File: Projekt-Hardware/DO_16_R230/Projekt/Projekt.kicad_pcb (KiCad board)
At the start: 2 copper layers, 131.6 x 142.2 mm, 41 parts, among them J1 COM_Bus, J2 COM_Bus, J4 Conn_01x02, J5 Conn_01x08, J6 Conn_01x08, K1 DIPxx-1Cxx-51x, K10 DIPxx-1Cxx-51x, K11 DIPxx-1Cxx-51x, K12 DIPxx-1Cxx-51x, K13 DIPxx-1Cxx-51x, K14 DIPxx-1Cxx-51x, K15 DIPxx-1Cxx-51x, K16 DIPxx-1Cxx-51x, K2 DIPxx-1Cxx-51x, K3 DIPxx-1Cxx-51x, K4 DIPxx-1Cxx-51x, K5 DIPxx-1Cxx-51x, K6 DIPxx-1Cxx-51x, K7 DIPxx-1Cxx-51x, K8 DIPxx-1Cxx-51x, K9 DIPxx-1Cxx-51x, SW1 RESET, U1 ATmega328P-PU

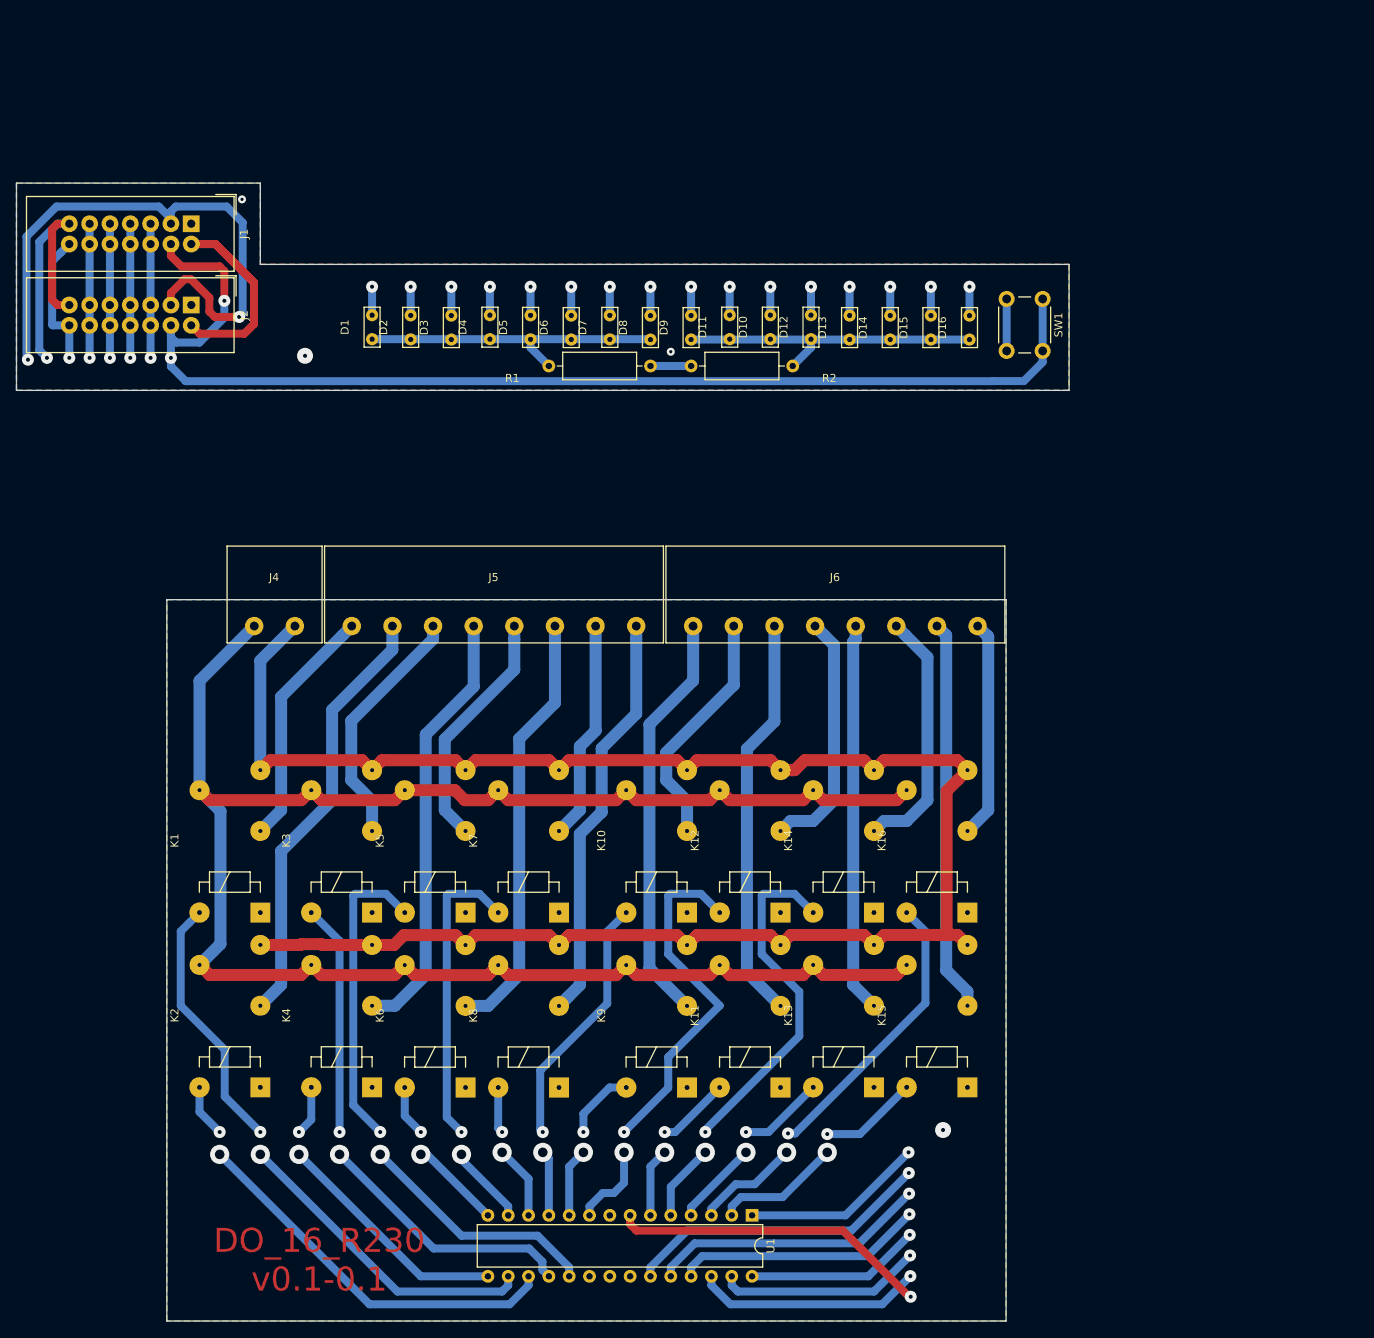
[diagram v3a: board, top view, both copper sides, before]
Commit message: Anpassungen Gehäuse + CNC Experimente
Anpassungen des Gehäuses an die Leiteplatte

Angefangen mit Tests für das herstellen der Leiterplatte mit einer CNC Fräse
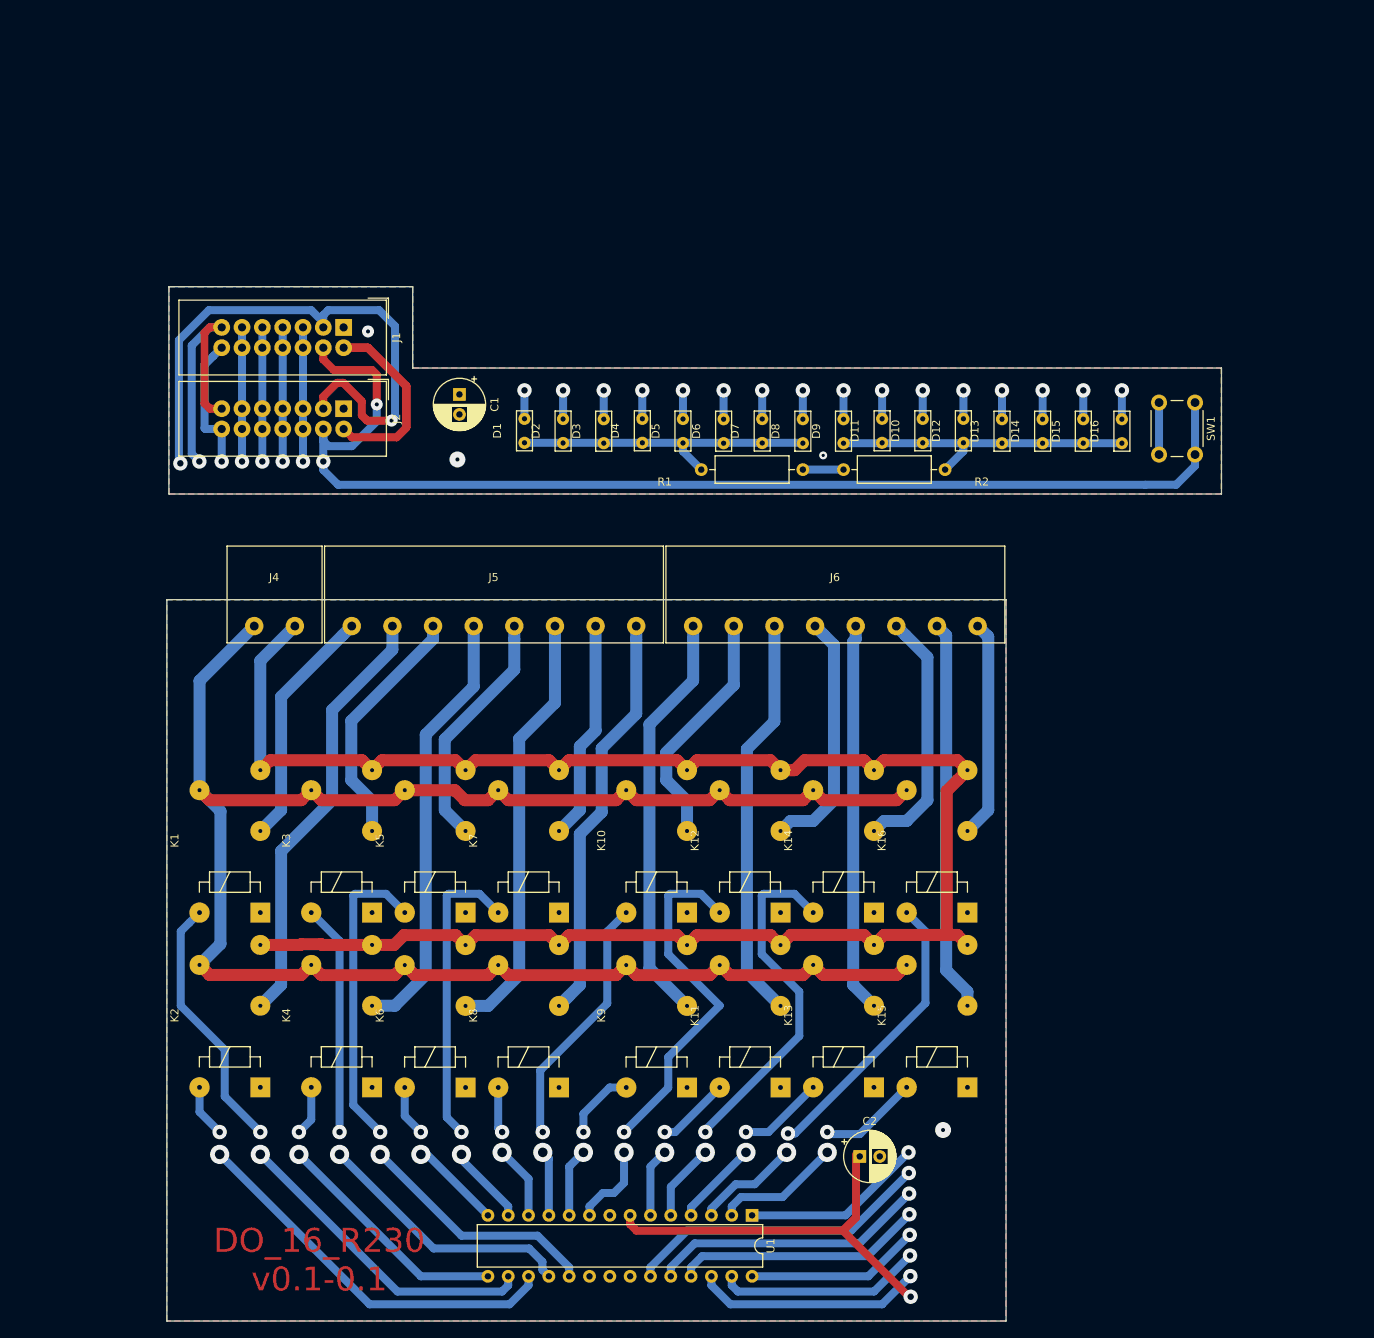
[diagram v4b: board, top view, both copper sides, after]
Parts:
- added C1: 10uF, Capacitor_THT:CP_Radial_D6.3mm_P2.50mm, F.Cu at (97.8, 71.9)
- added C2: 10uF, Capacitor_THT:CP_Radial_D6.3mm_P2.50mm, F.Cu at (147.8, 167.1)
- moved D1 23.0 mm to (105.9, 76.4)
- moved D10 23.0 mm to (155.7, 76.4)
- moved D11 23.0 mm to (150.6, 76.4)
- moved D12 23.0 mm to (160.8, 76.4)
- moved D4 23.0 mm to (120.7, 76.4)
- moved R2 23.0 mm to (158.5, 81.3)
- moved D13 23.0 mm to (165.6, 76.5)
- moved D15 23.0 mm to (175.8, 76.5)
- moved D8 23.0 mm to (140.7, 76.5)
- moved SW1 23.0 mm to (189.7, 72.9)
- moved R1 23.0 mm to (128.0, 81.3)
- moved J1 23.0 mm to (83.3, 63.5)
- moved D2 23.0 mm to (110.7, 76.5)
- moved D3 23.0 mm to (115.8, 76.5)
- moved D5 23.0 mm to (125.7, 76.5)
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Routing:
- net Net-(C2-Pad1): track 78.8 -> 89.0 mm
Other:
- board size 131.6 x 142.2 mm -> 131.8 x 129.3 mm

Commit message: Hardware CNC Codes erstellt
Fertigungsdateien für eine CNC Version der
Leiterplatten erstellt.
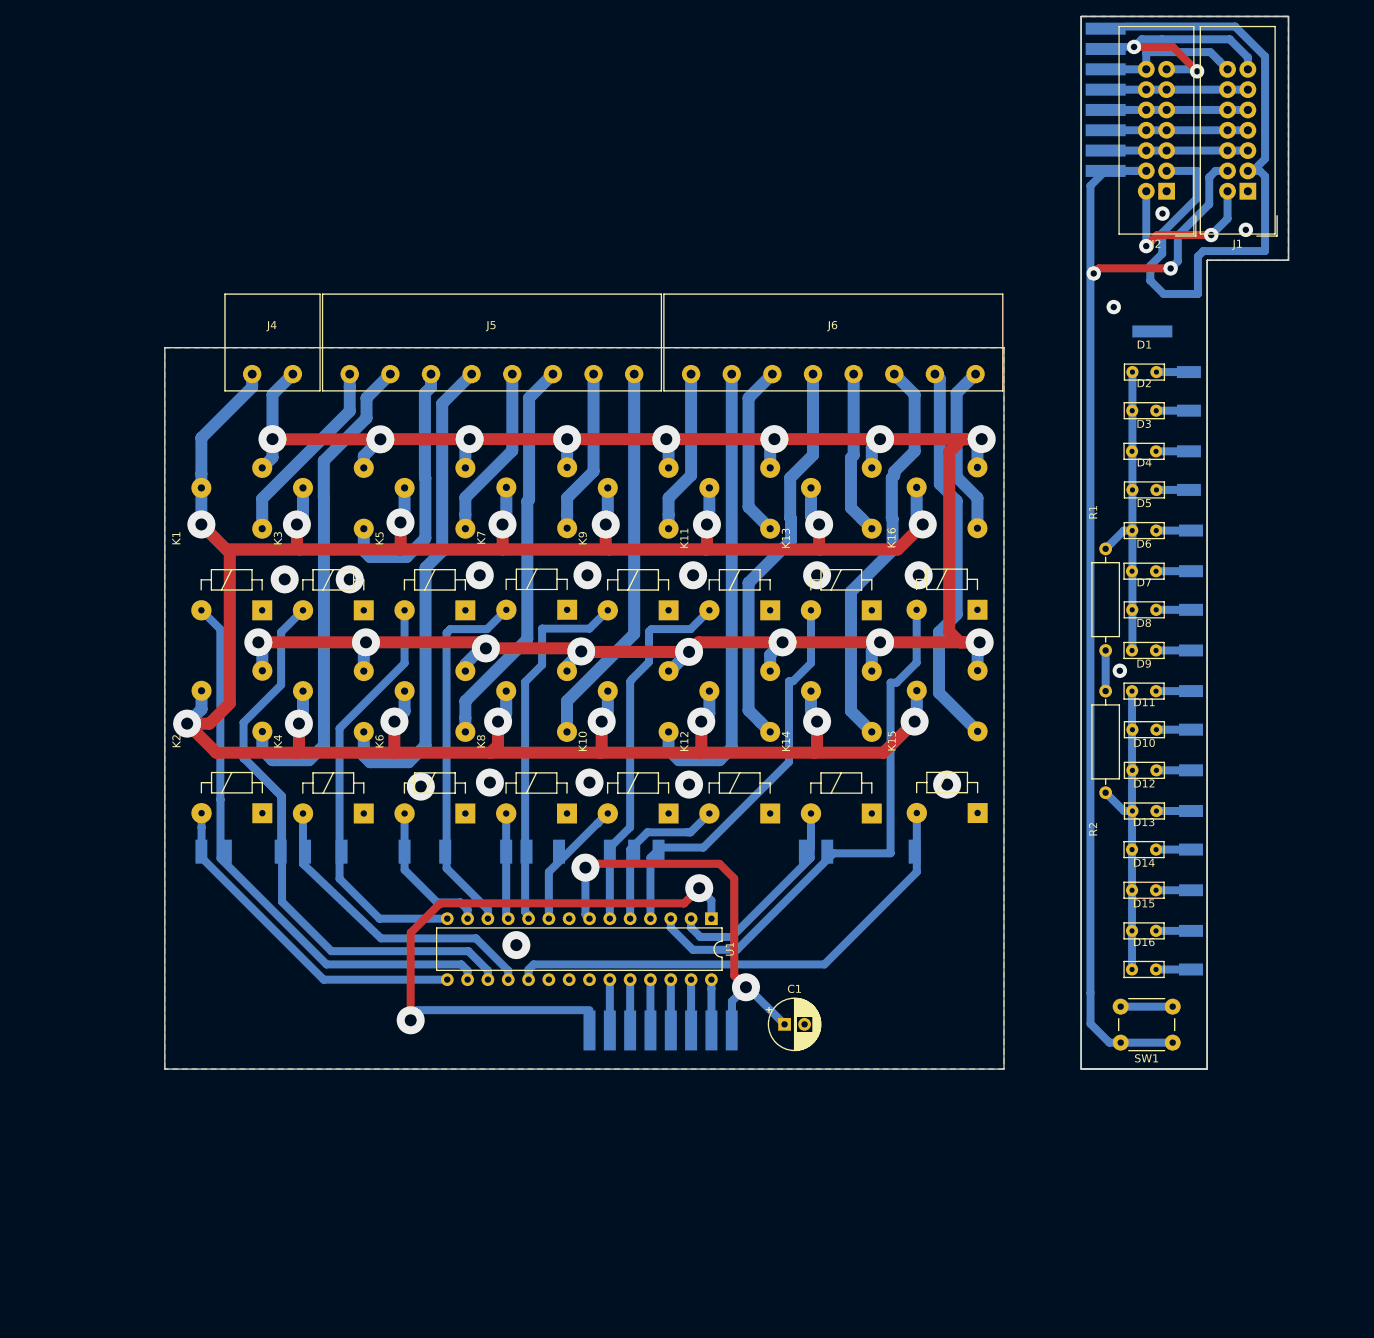
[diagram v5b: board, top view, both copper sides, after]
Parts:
- removed C2: 10uF, Capacitor_THT:CP_Radial_D6.3mm_P2.50mm
- added REF**: SM_SolderPad_1.5x3, Footprints:SM_SolderPad_1.5x3, B.Cu at (189.0, 73.9)
- added REF**: SM_SolderPad_1.5x5, Footprints:SM_SolderPad_1.5x5, B.Cu at (178.6, 33.8)
- added REF**: SM_SolderPad_1.5x5, Footprints:SM_SolderPad_1.5x5, B.Cu at (178.6, 31.2)
- added REF**: SM_SolderPad_1.5x3, Footprints:SM_SolderPad_1.5x3, B.Cu at (189.2, 118.9)
- added REF**: SM_SolderPad_1.5x3, Footprints:SM_SolderPad_1.5x3, B.Cu at (189.2, 109.0)
- added REF**: SM_SolderPad_1.5x3, Footprints:SM_SolderPad_1.5x3, B.Cu at (189.2, 98.8)
- added REF**: SM_SolderPad_1.5x3, Footprints:SM_SolderPad_1.5x3, B.Cu at (189.2, 94.0)
- added REF**: SM_SolderPad_1.5x3, Footprints:SM_SolderPad_1.5x3, B.Cu at (189.2, 103.9)
- added REF**: SM_SolderPad_1.5x3, Footprints:SM_SolderPad_1.5x3, B.Cu at (189.0, 83.8)
- added REF**: SM_SolderPad_1.5x3, Footprints:SM_SolderPad_1.5x3, B.Cu at (189.0, 69.1)
- added REF**: SM_SolderPad_1.5x5, Footprints:SM_SolderPad_1.5x5, B.Cu at (178.6, 43.9)
- added REF**: SM_SolderPad_1.5x3, Footprints:SM_SolderPad_1.5x3, B.Cu at (189.2, 113.8)
- added REF**: SM_SolderPad_1.5x5, Footprints:SM_SolderPad_1.5x5, B.Cu at (184.4, 64.0)
- added REF**: SM_SolderPad_1.5x3, Footprints:SM_SolderPad_1.5x3, B.Cu at (189.2, 143.8)
- added REF**: SM_SolderPad_1.5x3, Footprints:SM_SolderPad_1.5x3, B.Cu at (189.2, 138.9)
- added REF**: SM_SolderPad_1.5x3, Footprints:SM_SolderPad_1.5x3, B.Cu at (189.2, 128.8)
- added REF**: SM_SolderPad_1.5x3, Footprints:SM_SolderPad_1.5x3, B.Cu at (189.2, 124.0)
- added REF**: SM_SolderPad_1.5x3, Footprints:SM_SolderPad_1.5x3, B.Cu at (189.2, 133.9)
- added REF**: SM_SolderPad_1.5x3, Footprints:SM_SolderPad_1.5x3, B.Cu at (122.7, 129.0)
- added REF**: SM_SolderPad_1.5x3, Footprints:SM_SolderPad_1.5x3, B.Cu at (65.5, 129.0)
- added REF**: SM_SolderPad_1.5x3, Footprints:SM_SolderPad_1.5x3, B.Cu at (119.6, 129.0)
- added REF**: SM_SolderPad_1.5x3, Footprints:SM_SolderPad_1.5x3, B.Cu at (75.4, 129.0)
- added REF**: SM_SolderPad_1.5x3, Footprints:SM_SolderPad_1.5x3, B.Cu at (189.2, 88.9)
- added REF**: SM_SolderPad_1.5x3, Footprints:SM_SolderPad_1.5x3, B.Cu at (110.2, 129.0)
- added REF**: SM_SolderPad_1.5x3, Footprints:SM_SolderPad_1.5x3, B.Cu at (116.6, 129.0)
- added REF**: SM_SolderPad_1.5x3, Footprints:SM_SolderPad_1.5x3, B.Cu at (106.2, 129.0)
- added REF**: SM_SolderPad_1.5x3, Footprints:SM_SolderPad_1.5x3, B.Cu at (103.6, 129.0)
- added REF**: SM_SolderPad_1.5x3, Footprints:SM_SolderPad_1.5x3, B.Cu at (143.8, 129.0)
- added REF**: SM_SolderPad_1.5x3, Footprints:SM_SolderPad_1.5x3, B.Cu at (78.5, 129.0)
- added REF**: SM_SolderPad_1.5x3, Footprints:SM_SolderPad_1.5x3, B.Cu at (154.7, 129.0)
- added REF**: SM_SolderPad_1.5x3, Footprints:SM_SolderPad_1.5x3, B.Cu at (68.6, 129.0)
- added REF**: SM_SolderPad_1.5x3, Footprints:SM_SolderPad_1.5x3, B.Cu at (83.1, 129.0)
- added REF**: SM_SolderPad_1.5x3, Footprints:SM_SolderPad_1.5x3, B.Cu at (141.0, 129.0)
- added REF**: SM_SolderPad_1.5x3, Footprints:SM_SolderPad_1.5x3, B.Cu at (189.0, 79.0)
- added REF**: SM_SolderPad_1.5x5, Footprints:SM_SolderPad_1.5x5, B.Cu at (129.3, 151.4)
- added REF**: SM_SolderPad_1.5x3, Footprints:SM_SolderPad_1.5x3, B.Cu at (90.9, 129.0)
- added REF**: SM_SolderPad_1.5x5, Footprints:SM_SolderPad_1.5x5, B.Cu at (126.7, 151.4)
- added REF**: SM_SolderPad_1.5x5, Footprints:SM_SolderPad_1.5x5, B.Cu at (121.7, 151.4)
- added REF**: SM_SolderPad_1.5x5, Footprints:SM_SolderPad_1.5x5, B.Cu at (124.2, 151.4)
- added REF**: SM_SolderPad_1.5x5, Footprints:SM_SolderPad_1.5x5, B.Cu at (114.0, 151.4)
- added REF**: SM_SolderPad_1.5x5, Footprints:SM_SolderPad_1.5x5, B.Cu at (116.6, 151.4)
- added REF**: SM_SolderPad_1.5x5, Footprints:SM_SolderPad_1.5x5, B.Cu at (119.1, 151.4)
- added REF**: SM_SolderPad_1.5x3, Footprints:SM_SolderPad_1.5x3, B.Cu at (96.0, 129.0)
- added REF**: SM_SolderPad_1.5x5, Footprints:SM_SolderPad_1.5x5, B.Cu at (131.8, 151.4)
- added REF**: SM_SolderPad_1.5x5, Footprints:SM_SolderPad_1.5x5, B.Cu at (178.6, 26.2)
- added REF**: SM_SolderPad_1.5x5, Footprints:SM_SolderPad_1.5x5, B.Cu at (178.6, 28.7)
- added REF**: SM_SolderPad_1.5x5, Footprints:SM_SolderPad_1.5x5, B.Cu at (178.6, 41.4)
- added REF**: SM_SolderPad_1.5x5, Footprints:SM_SolderPad_1.5x5, B.Cu at (178.6, 38.9)
- added REF**: SM_SolderPad_1.5x5, Footprints:SM_SolderPad_1.5x5, B.Cu at (178.6, 36.3)
- moved J1 114.3 mm to (196.3, 46.5), turned to 180 degrees
- moved J2 106.4 mm to (186.2, 46.5), turned to 180 degrees
- moved C1 88.6 mm to (138.4, 150.6), turned to 0 degrees
- moved SW1 80.1 mm to (186.9, 152.9), turned to 180 degrees
- moved D1 77.8 mm to (183.4, 69.1), turned to 0 degrees
- moved D2 72.7 mm to (183.4, 73.9), turned to 0 degrees
- moved D3 67.6 mm to (183.4, 79.0), turned to 0 degrees
- moved D16 67.3 mm to (183.4, 143.8), turned to 0 degrees
- moved D4 63.2 mm to (183.4, 83.8), turned to 0 degrees
- moved D15 62.9 mm to (183.4, 138.9), turned to 0 degrees
- moved K9 59.7 mm to (123.9, 98.9)
- moved K11 59.7 mm to (136.6, 98.9)
- moved K13 59.6 mm to (149.3, 98.9)
- moved D5 59.0 mm to (183.4, 88.9), turned to 0 degrees
- moved D14 58.8 mm to (183.4, 133.9), turned to 0 degrees
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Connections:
- net Net-(J1-Pad10) renamed /COM_OUT_1
- net Net-(J1-Pad11) renamed /COM_OUT_2
- net Net-(J1-Pad13) renamed /CLOCK
- net Net-(J1-Pad14) renamed /ENABLE
- net Net-(J1-Pad5) renamed /COM_IN_1
- net Net-(J1-Pad7) renamed /COM_IN_2
- C1 pad 1: Net-(C1-Pad1) -> /+5V
- C1 pad 2: Net-(C1-Pad2) -> /GND
- J1 pad 1: Net-(C1-Pad1) -> /GND
- J1 pad 2: Net-(C2-Pad1) -> /+5V
- J1 pad 3: Net-(C1-Pad2) -> /-5V
- J1 pad 4: Net-(J1-Pad4) -> /RESET
- J2 pad 1: Net-(C1-Pad1) -> /GND
- J2 pad 2: Net-(C2-Pad1) -> /+5V
- J2 pad 3: Net-(C1-Pad2) -> /-5V
- J2 pad 4: Net-(J1-Pad4) -> /RESET
- K1 pad 6: Net-(C1-Pad1) -> /GND
- K10 pad 6: Net-(C1-Pad1) -> /GND
- K11 pad 6: Net-(C1-Pad1) -> /GND
- K12 pad 6: Net-(C1-Pad1) -> /GND
- K13 pad 6: Net-(C1-Pad1) -> /GND
- K14 pad 6: Net-(C1-Pad1) -> /GND
- K15 pad 6: Net-(C1-Pad1) -> /GND
- K16 pad 6: Net-(C1-Pad1) -> /GND
- K2 pad 6: Net-(C1-Pad1) -> /GND
- K3 pad 6: Net-(C1-Pad1) -> /GND
- K4 pad 6: Net-(C1-Pad1) -> /GND
- K5 pad 6: Net-(C1-Pad1) -> /GND
- K6 pad 6: Net-(C1-Pad1) -> /GND
- K7 pad 6: Net-(C1-Pad1) -> /GND
- K8 pad 6: Net-(C1-Pad1) -> /GND
- K9 pad 6: Net-(C1-Pad1) -> /GND
- R1 pad 2: Net-(C1-Pad1) -> /GND
- R2 pad 2: Net-(C1-Pad1) -> /GND
- SW1 pad 1: Net-(J1-Pad4) -> /RESET
- SW1 pad 2: Net-(C1-Pad1) -> /GND
- U1 pad 1: Net-(J1-Pad4) -> /RESET
- U1 pad 10: Net-(D8-Pad2) -> Net-(D9-Pad2)
- U1 pad 11: Net-(D14-Pad2) -> Net-(D8-Pad2)
- U1 pad 12: Net-(D15-Pad2) -> Net-(D7-Pad2)
- U1 pad 13: Net-(D16-Pad2) -> Net-(D6-Pad2)
- U1 pad 14: Net-(D1-Pad2) -> Net-(D5-Pad2)
- U1 pad 16: Net-(D3-Pad2) -> Net-(D1-Pad2)
- U1 pad 17: Net-(D4-Pad2) -> Net-(D3-Pad2)
- U1 pad 18: Net-(D5-Pad2) -> Net-(D4-Pad2)
- U1 pad 19: Net-(D6-Pad2) -> Net-(D15-Pad2)
- U1 pad 2: Net-(D9-Pad2) -> Net-(D14-Pad2)
- U1 pad 22: Net-(C1-Pad1) -> /GND
- U1 pad 3: Net-(D10-Pad2) -> Net-(D16-Pad2)
- U1 pad 4: Net-(D11-Pad2) -> Net-(D13-Pad2)
- U1 pad 6: Net-(D13-Pad2) -> Net-(D11-Pad2)
- U1 pad 7: Net-(C2-Pad1) -> /+5V
- U1 pad 8: Net-(C1-Pad1) -> /GND
- U1 pad 9: Net-(D7-Pad2) -> Net-(D10-Pad2)
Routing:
- net Net-(J4-Pad1): track 238.7 -> 345.1 mm, vias 0 -> 16
- net Net-(C2-Pad1): track 89.0 -> 0.00 mm, vias 1 -> 0
- net /-5V: track 0.00 -> 86.2 mm
- net /RESET: track 0.00 -> 74.8 mm, vias 0 -> 2
- net /+5V: track 0.00 -> 74.6 mm, vias 0 -> 4
- net Net-(C1-Pad2): track 73.6 -> 0.00 mm, vias 2 -> 0
- net /COM_OUT_1: track 55.1 -> 5.59 mm, vias 2 -> 0
- net Net-(J4-Pad2): track 231.8 -> 280.9 mm, vias 0 -> 16
- net /COM_OUT_2: track 51.5 -> 5.59 mm, vias 2 -> 0
- net /COM_IN_1: track 47.9 -> 5.59 mm, vias 2 -> 0
- net Net-(D15-Pad2): track 25.2 -> 65.8 mm, vias 3 -> 0
- net /COM_IN_2: track 45.2 -> 5.84 mm, vias 2 -> 0
- net Net-(D12-Pad2): track 57.9 -> 24.4 mm, vias 3 -> 0
- net /ENABLE: track 39.1 -> 5.84 mm, vias 2 -> 0
- net Net-(J6-Pad1): track 51.7 -> 20.5 mm
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- added copper zone on B.Cu, net /GND
- added copper zone on F.Cu, net /GND
- removed copper zone on B.Cu, net Net-(C1-Pad1)
- removed copper zone on F.Cu, net Net-(C1-Pad1)
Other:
- board size 131.8 x 129.3 mm -> 140.5 x 131.6 mm
- board text removed: "DO_16_R230 v0.1-0.1"
